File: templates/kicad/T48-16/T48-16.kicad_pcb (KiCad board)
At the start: 2 copper layers, 4 x 8 mm, 16 parts

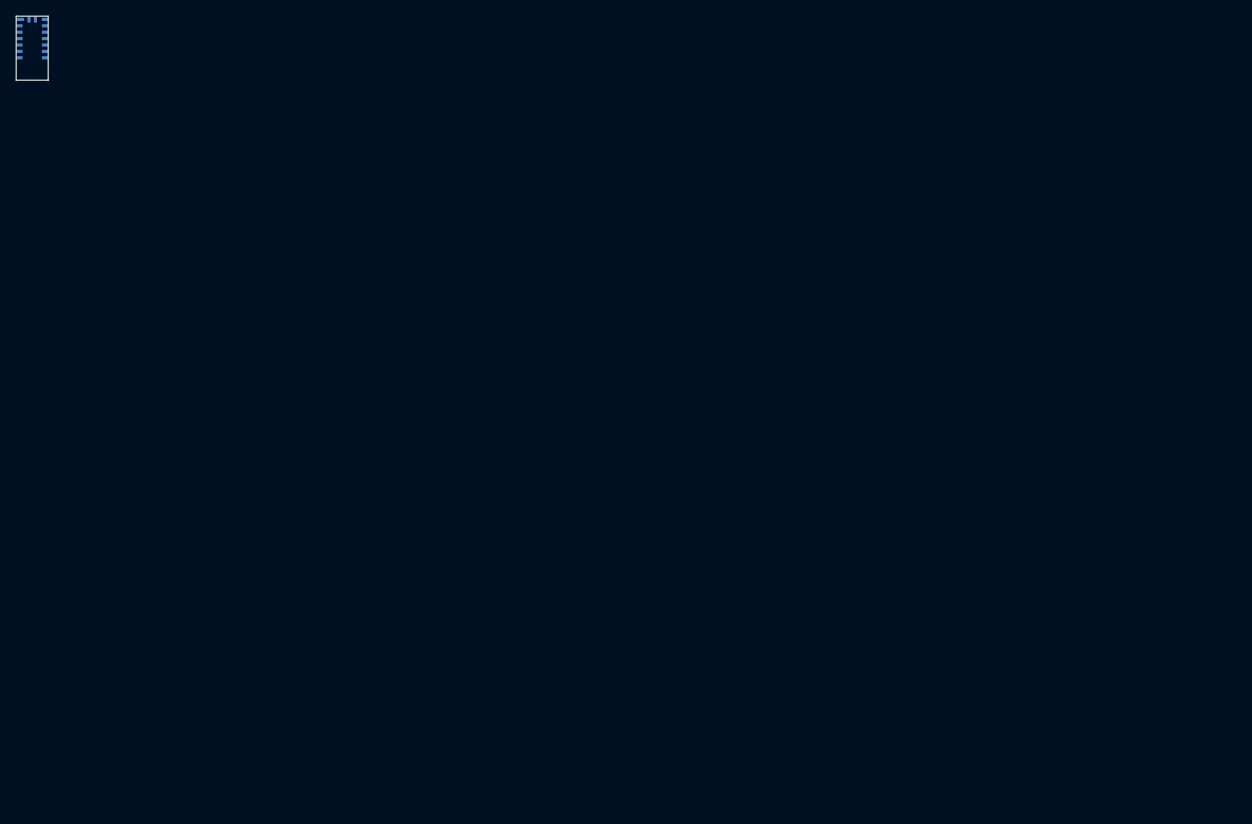
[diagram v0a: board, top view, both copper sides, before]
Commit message: Adding pin numbers to pads in template files.
Another way to have iterating pads would have been to add one N-pin header, but that would lock all the pads to one location on the schematic, not ideal. The other would have been to create 22 custom schematic pin symbols, iterating the pad numbers in there. But that would duplicate pad structures. Much more elegant (imho) to have the pads be labelled in the user comments layer.
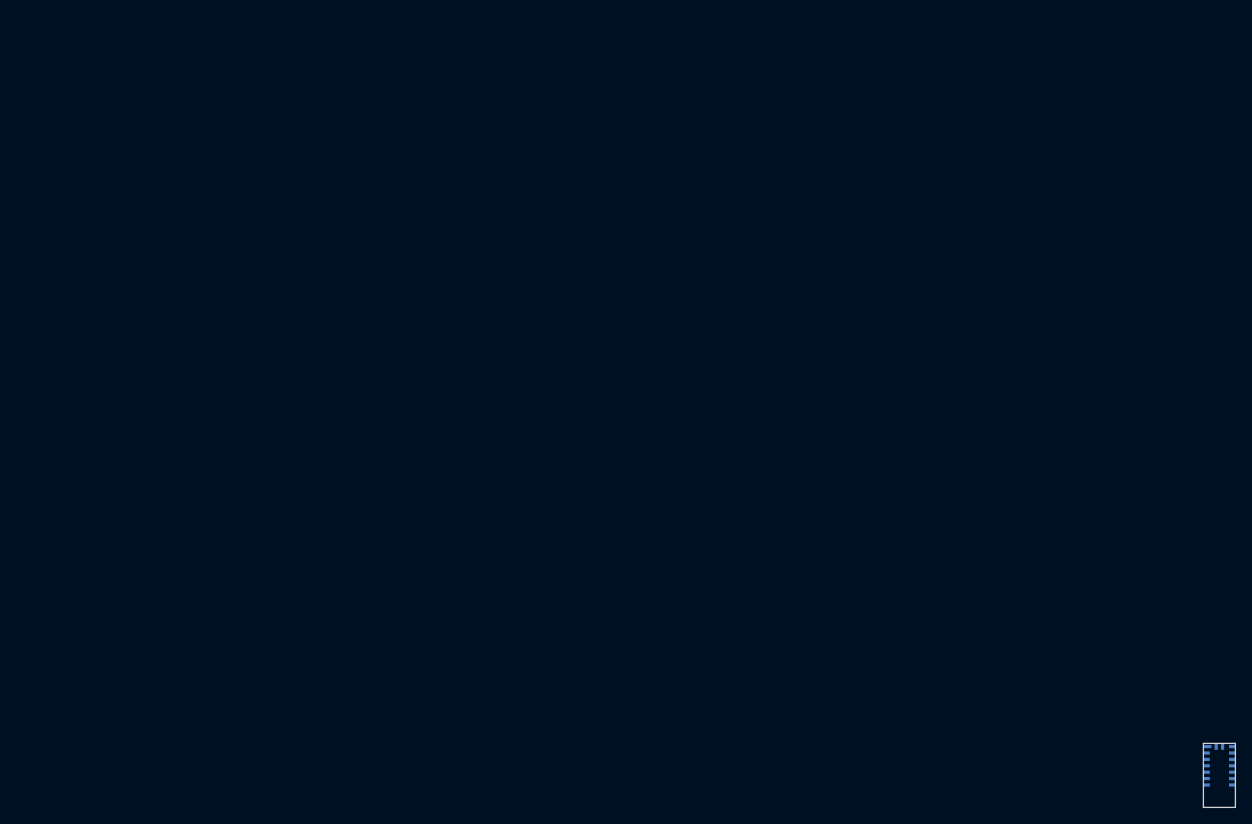
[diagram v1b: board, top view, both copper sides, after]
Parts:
- moved P1 174.0 mm to (146.9, 89.3)
- moved P10 174.0 mm to (150.0, 92.5)
- moved P11 174.0 mm to (150.0, 91.7)
- moved P12 174.0 mm to (150.0, 90.9)
- moved P13 174.0 mm to (150.0, 90.1)
- moved P14 174.0 mm to (150.0, 89.3)
- moved P15 174.0 mm to (148.8, 89.3)
- moved P16 174.0 mm to (148.0, 89.3)
- moved P2 174.0 mm to (146.8, 90.1)
- moved P3 174.0 mm to (146.8, 90.9)
- moved P4 174.0 mm to (146.8, 91.7)
- moved P5 174.0 mm to (146.8, 92.5)
- moved P6 174.0 mm to (146.8, 93.3)
- moved P7 174.0 mm to (146.8, 94.1)
- moved P8 174.0 mm to (150.0, 94.1)
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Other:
- board text added: "P1"
- board text added: "P10"
- board text added: "P11"
- board text added: "P12"
- board text added: "P13"
- board text added: "P14"
- board text added: "P15"
- board text added: "P16"
- board text added: "P2"
- board text added: "P3"
- board text added: "P4"
- board text added: "P5"
- board text added: "P6"
- board text added: "P7"
- board text added: "P8"
- board text added: "P9"
